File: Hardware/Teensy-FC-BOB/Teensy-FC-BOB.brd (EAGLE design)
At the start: 100 x 80 mm, 2 parts

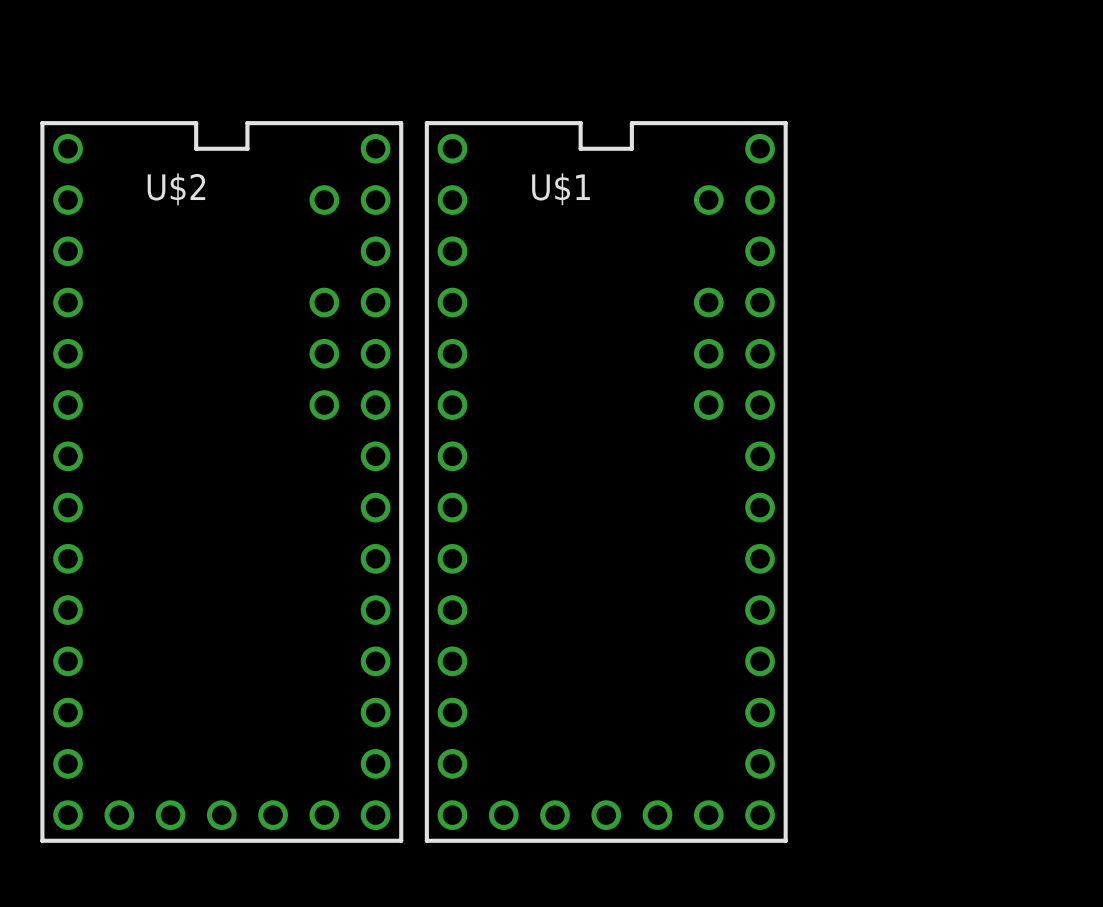
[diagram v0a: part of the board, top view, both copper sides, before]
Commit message: added the 10dof to the bob
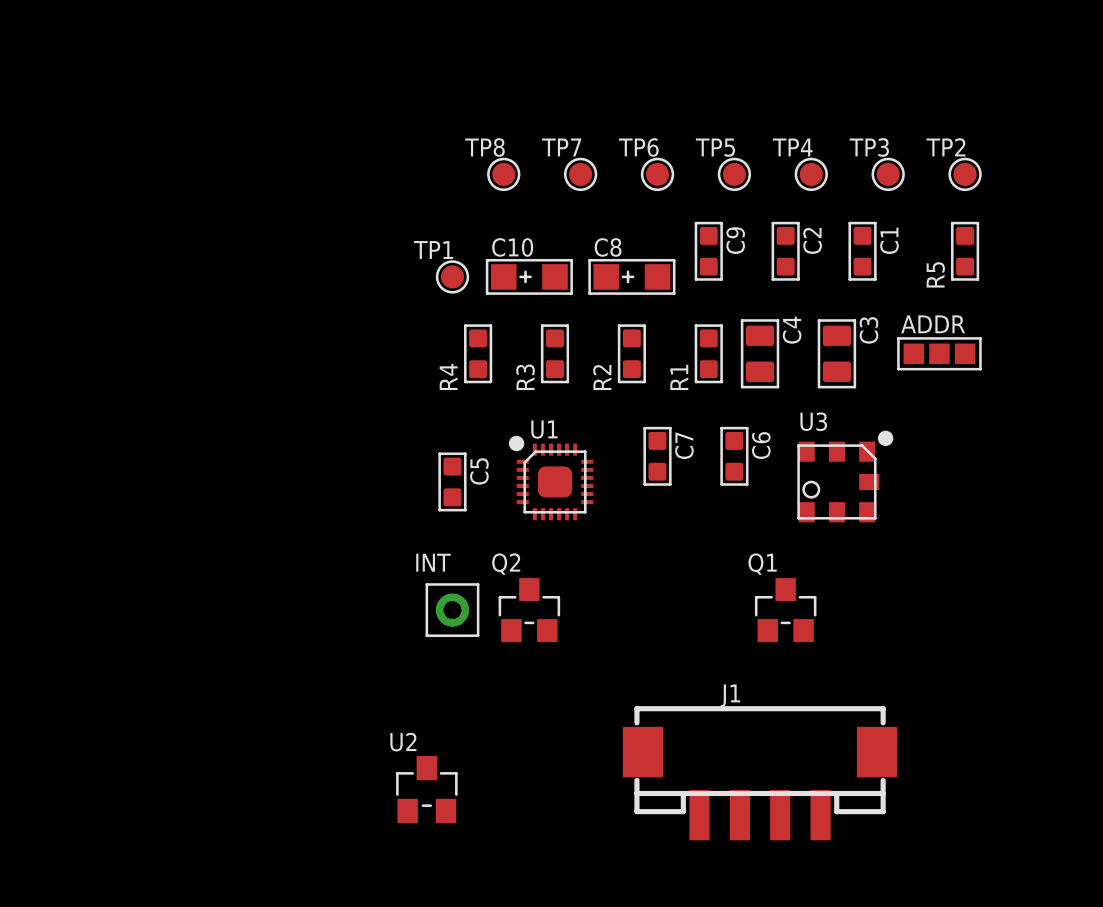
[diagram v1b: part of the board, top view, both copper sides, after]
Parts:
- removed U$1, U$2: TEENSY_3.1_ALL_PINS, Teensy_3_and_LC_Series_Boards_v1.0:TEENSY3-ALL_PINS
- added ADDR: DNP, Discrete-new:3P-SMD-L4.1*W1.5MM
- added C1, C2, C9: 100nF, Discrete-new:C0603
- added C10, C8: DNP, Discrete-new:AVX-A
- added C3, C4: 10uF, Discrete-new:C0805
- added C5: 10nF 10%, Discrete-new:C0603
- added C6, C7: 100nF 10%, Discrete-new:C0603
- added INT: DNP, Connector-new:1P-65/35MIL
- added J1: 4P-2.0;320110030, Connector-new:4P-SMD-2.0
- added Q1, Q2: 2N7002;305030028, Discrete-new:SOT-23
- added R1, R2, R3, R4: 10k, Discrete-new:R0603
- added R5: 4.7k, Discrete-new:R0603
- added TP1, TP2, TP3, TP4, TP5, TP6, TP7, TP8: DNP, Discrete-new:TP-D45MIL
- added U1: MPU-9250, template:LEAD-QFN24
- added U2: XC6206P332MR-G, IC-new:SOT-23
- added U3: BMP180;314030004, template:LGA-7
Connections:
- removed net 3.3V: U$1.3.3V, U$1.3.3V1, U$2.3.3V, U$2.3.3V1
- removed net AGND: U$1.AGND, U$2.AGND
- removed net AREF: U$1.AREF, U$2.AREF
- removed net VBAT: U$1.VBAT, U$2.VBAT
- removed net VIN: U$1.VIN, U$2.VIN
- removed net VUSB: U$1.VUSB, U$2.VUSB
- new net AD0/SDO: ADDR.MM, U1.9
- new net N$3: C6.1, U1.10
- new net N$4: INT.1, R5.2, U1.12
- new net SCL/SCLK: Q1.2, R1.2, TP6.T, U1.23, U3.5
- new net SCL_H: J1.1, Q1.3, R4.2, TP4.T
- new net SDA/SDI: Q2.2, R2.2, TP7.T, U1.24, U3.6
- new net SDA_H: J1.2, Q2.3, R3.2, TP3.T
- new net VCC: C1.2, C3.2, J1.3, R3.1, R4.1, TP2.T, U2.3
- new net VCC_3V3: ADDR.00, C10.+, C2.2, C4.2, C5.1, C7.2, C8.+, C9.1, Q1.1, Q2.1, R1.1, R2.1, R5.1, TP5.T, U1.1, U1.13, U1.22, U1.8, U2.2, U3.2, U3.3
- net GND: now also ADDR.11, C1.1, C10.-, C2.1, C3.1, C4.1, C5.2, C6.2, C7.1, C8.-, C9.2, J1.4, J1.SS1, J1.SS2, TP1.T, U1.11, U1.18, U1.20, U2.1, U3.7; no longer U$1.GND, U$1.GND1, U$2.GND, U$2.GND1
